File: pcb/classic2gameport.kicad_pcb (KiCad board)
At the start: 2 copper layers, 58 x 45 mm, 39 parts, among them J1 DB15_Male, J2 AVR-ISP-10, J3 Conn_01x04, Q1 Q_PMOS_GSD, Q2 Q_PMOS_GSD, Q3 Q_PMOS_GSD, Q4 Q_PMOS_GSD, Q5 Q_PMOS_GSD, Q6 Q_PMOS_GSD, Q7 Q_PMOS_GSD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

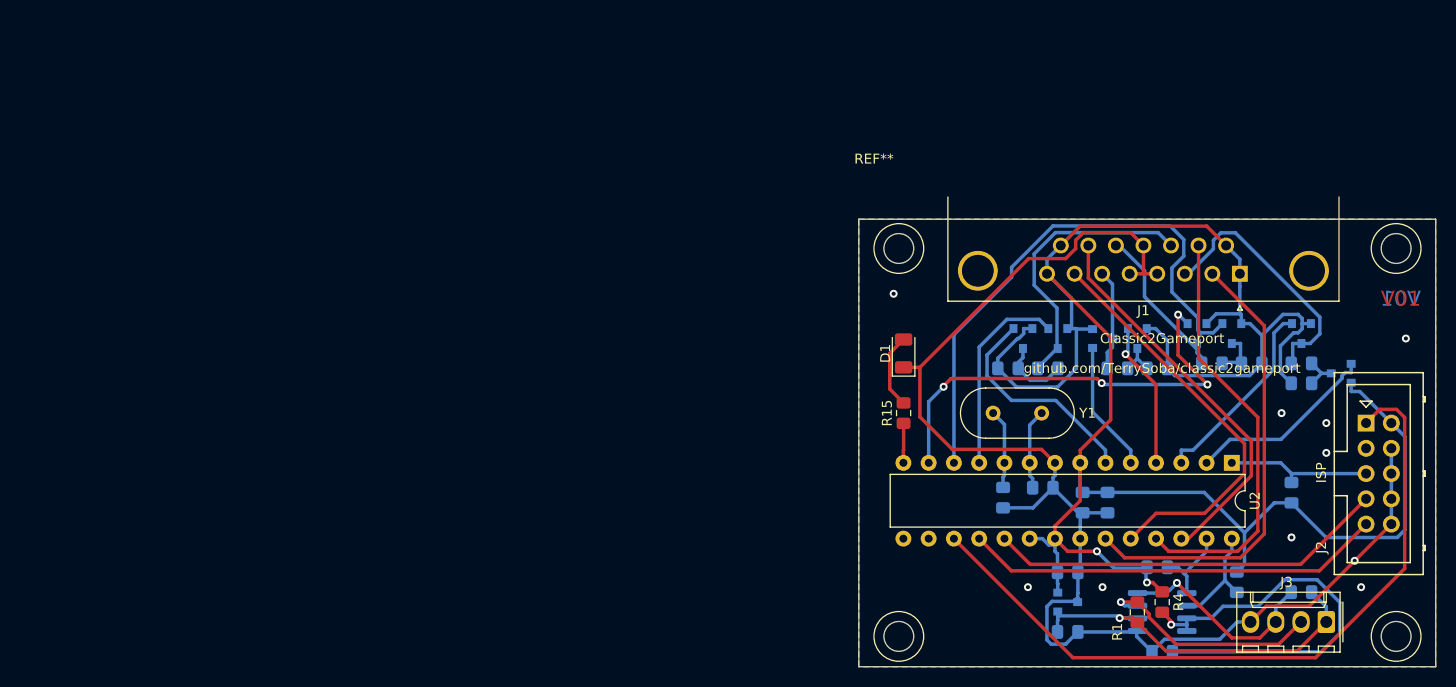
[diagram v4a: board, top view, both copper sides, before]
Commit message: Change to STM32 MCU
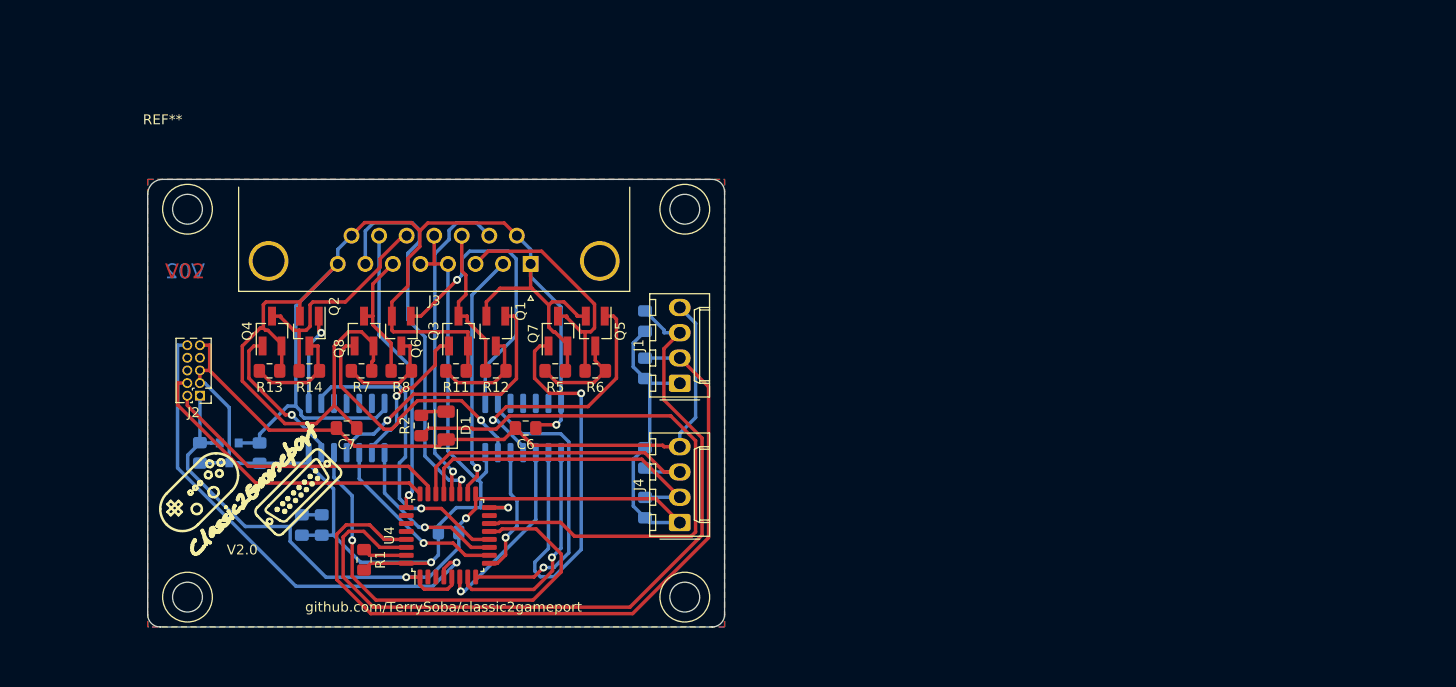
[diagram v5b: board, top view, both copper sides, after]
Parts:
- removed R15: 1.2k, Resistor_SMD:R_0805_2012Metric_Pad1.15x1.40mm_HandSolder
- removed Y1: 16MHz, Crystal:Crystal_HC49-4H_Vertical
- added J4: Conn_01x04, Connector_Molex:Molex_KK-254_AE-6410-04A_1x04_P2.54mm_Vertical, F.Cu at (138.0, 72.0)
- added U4: STM32F030K6Tx, Package_QFP:LQFP-32_7x7mm_P0.8mm, F.Cu at (114.7, 73.3)
- C3: value 22pF -> 1µF
- C4: value 22pF -> 4.7µF
- C6: value 1µF -> 100nF; moved to F.Cu
- C7, R11, R12, R13, R14, R7, R8: moved to F.Cu
- J1: value DB15_Male -> Conn_01x04; footprint Connector_Dsub:DSUB-15_Male_Horizontal_P2.77x2.84mm_EdgePinOffset4.94mm_Housed_MountingHolesOffset7.48mm -> Connector_Molex:Molex_KK-254_AE-6410-04A_1x04_P2.54mm_Vertical
- J2: value AVR-ISP-10 -> Conn_02x05_Odd_Even; footprint Connector_Multicomp:Multicomp_MC9A12-1034_2x05_P2.54mm_Vertical -> Connector_PinHeader_1.27mm:PinHeader_2x05_P1.27mm_Vertical
- J3: value Conn_01x04 -> DB15_Male; footprint Connector_Molex:Molex_KK-254_AE-6410-04A_1x04_P2.54mm_Vertical -> Connector_Dsub:DSUB-15_Male_Horizontal_P2.77x2.84mm_EdgePinOffset4.94mm_Housed_MountingHolesOffset7.48mm
- Q1, Q2, Q3, Q4, Q5, Q6, Q7, Q8: footprint Package_TO_SOT_SMD:SOT-23 -> Package_TO_SOT_SMD:SOT-23_Handsoldering; moved to F.Cu
- R1: value 1kR -> 10k
- R10, R9: value 49k9 -> 1kR
- R2: value 1kR -> 470R; moved to F.Cu
- R3: value 10kR -> 1kR
- R4: value 200kR -> 1kR; moved to B.Cu
- R5, R6: value 1kR -> 49k9; moved to F.Cu
- U1: value LM3480-3.3 -> 74HC14; footprint Package_TO_SOT_SMD:SOT-23 -> Package_SO:SOIC-14_3.9x8.7mm_P1.27mm
- U2: value ATmega8-16PU -> 74HC14; footprint Package_DIP:DIP-28_W7.62mm -> Package_SO:SOIC-14_3.9x8.7mm_P1.27mm; moved to B.Cu
- U3: value PCA9306 -> LM3480-3.3; footprint Package_SO:SOIC-8_3.9x4.9mm_P1.27mm -> Package_TO_SOT_SMD:SOT-23
- moved J2 117.3 mm to (89.8, 59.2), turned to 180 degrees
- moved R13 98.8 mm to (96.8, 56.8)
- moved U3 95.2 mm to (92.7, 65.0), turned to 270 degrees
- moved R7 94.5 mm to (106.0, 56.8), turned to 180 degrees
- moved R14 90.8 mm to (100.8, 56.8)
- moved R8 90.5 mm to (110.0, 56.8)
- moved R2 90.1 mm to (112.0, 62.2), turned to 90 degrees
- moved U2 89.1 mm to (104.5, 62.5), turned to 90 degrees
- moved C2 88.9 mm to (89.8, 65.0)
- moved J3 87.7 mm to (123.0, 46.0)
- moved Q1 85.1 mm to (119.5, 52.8), turned to 270 degrees
- moved C7 85.0 mm to (104.5, 62.5)
- moved Q3 84.8 mm to (115.8, 52.8), turned to 90 degrees
- moved Q8 83.8 mm to (106.2, 52.8), turned to 90 degrees
- moved Q4 83.5 mm to (97.0, 52.8), turned to 90 degrees
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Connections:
- C1 pad 1: 3.3V -> 5V
- C2 pad 1: 5V -> 3.3V
- C3 pad 1: Net-(C3-Pad1) -> 3.3V
- C4 pad 1: GND -> 3.3V
- C4 pad 2: Net-(C4-Pad2) -> GND
- C5 pad 1: 5V -> 3.3V
- C7 pad 1: Net-(C7-Pad1) -> 5V
- J1 pad 1: 5V -> 3.3V
- J1 pad 2: BUTTON1 -> SCL
- J1 pad 3: JS1_X_AXIS -> SDA
- J2 pad 1: MOSI -> 3.3V
- J2 pad 10: GND -> NRST
- J2 pad 2: 5V -> SWDIO
- J2 pad 3: Net-(J2-Pad3) -> GND
- J2 pad 4: GND -> SWCLK
- J2 pad 5: RESET -> GND
- J2 pad 6: GND -> (no net)
- J2 pad 7: SCK -> (no net)
- J2 pad 8: GND -> (no net)
- J2 pad 9: MISO -> GND
- J3 pad 1: 3.3V -> 5V
- J3 pad 2: Net-(J3-Pad2) -> BUTTON1
- J3 pad 3: Net-(J3-Pad3) -> JS1_X_AXIS
- Q1 pad 1: JS1_X1 -> Net-(Q1-Pad1)
- Q2 pad 1: JS1_Y1 -> Net-(Q2-Pad1)
- Q3 pad 1: JS1_X2 -> Net-(Q3-Pad1)
- Q3 pad 3: JS1_X_AXIS -> JS2_X_AXIS
- Q4 pad 1: JS1_Y2 -> Net-(Q4-Pad1)
- Q4 pad 3: JS1_Y_AXIS -> JS2_Y_AXIS
- Q5 pad 1: JS2_X1 -> Net-(Q5-Pad1)
- Q6 pad 1: JS2_Y1 -> Net-(Q6-Pad1)
- Q7 pad 1: JS2_X2 -> Net-(Q7-Pad1)
- Q7 pad 3: JS2_X_AXIS -> JS1_X_AXIS
- Q8 pad 1: JS2_Y2 -> Net-(Q8-Pad1)
- Q8 pad 3: JS2_Y_AXIS -> JS1_Y_AXIS
- R1 pad 1: 3.3V -> Net-(R1-Pad1)
- R1 pad 2: Net-(J3-Pad2) -> GND
- R10 pad 1: Net-(Q2-Pad3) -> 3.3V
- R10 pad 2: JS1_Y_AXIS -> SDA2
- R11 pad 2: Net-(Q5-Pad3) -> Net-(Q1-Pad3)
- R12 pad 1: Net-(Q5-Pad3) -> Net-(Q1-Pad3)
- R13 pad 2: Net-(Q6-Pad3) -> Net-(Q2-Pad3)
- R14 pad 1: Net-(Q6-Pad3) -> Net-(Q2-Pad3)
- R2 pad 1: 3.3V -> Net-(R2-Pad1)
- R2 pad 2: Net-(J3-Pad3) -> Net-(D1-Pad2)
- R3 pad 1: 5V -> 3.3V
- R3 pad 2: RESET -> SCL
- R4 pad 1: 5V -> 3.3V
- R4 pad 2: Net-(C7-Pad1) -> SDA
- R5 pad 2: SCL -> Net-(Q5-Pad3)
- R6 pad 1: 5V -> Net-(Q5-Pad3)
- R6 pad 2: SDA -> JS1_X_AXIS
- R7 pad 2: Net-(Q1-Pad3) -> Net-(Q6-Pad3)
- R8 pad 1: Net-(Q1-Pad3) -> Net-(Q6-Pad3)
- R8 pad 2: JS1_X_AXIS -> JS1_Y_AXIS
- R9 pad 1: 5V -> 3.3V
- R9 pad 2: Net-(Q2-Pad3) -> SCL2
- U1 pad 1: 3.3V -> JS1_X2
- U1 pad 2: 5V -> Net-(Q7-Pad1)
- U1 pad 3: GND -> JS1_X1
- U2 pad 1: RESET -> JS2_X2
- U2 pad 10: Net-(C4-Pad2) -> (no net)
- U2 pad 11: JS2_X2 -> (no net)
- U2 pad 12: JS2_Y1 -> (no net)
- U2 pad 13: JS2_Y2 -> (no net)
- U2 pad 14: Net-(R15-Pad1) -> 5V
- U2 pad 2: JS1_X1 -> Net-(Q3-Pad1)
- U2 pad 3: JS1_X2 -> JS2_X1
- U2 pad 4: JS1_Y1 -> Net-(Q1-Pad1)
- U2 pad 5: JS1_Y2 -> JS2_Y2
- U2 pad 6: JS2_X1 -> Net-(Q4-Pad1)
- U2 pad 7: 5V -> GND
- U2 pad 8: GND -> Net-(Q2-Pad1)
- U2 pad 9: Net-(C3-Pad1) -> JS2_Y1
- U3 pad 1: GND -> 3.3V
- U3 pad 2: 3.3V -> 5V
- U3 pad 3: Net-(J3-Pad2) -> GND
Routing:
- net MOSI: track 74.0 -> 0.00 mm
- net 3.3V: track 37.1 -> 109.4 mm, vias 1 -> 2
- net SDA: track 8.47 -> 78.8 mm
- net SCL: track 11.1 -> 77.3 mm
- net Net-(R2-Pad1): track 0.00 -> 60.2 mm
- net NRST: track 0.00 -> 49.7 mm, vias 0 -> 1
- net Net-(Q7-Pad1): track 0.00 -> 43.9 mm, vias 0 -> 1
- net Net-(C7-Pad1): track 43.1 -> 0.00 mm, vias 1 -> 0
- net MISO: track 42.2 -> 0.00 mm
- net SCK: track 40.2 -> 0.00 mm
- net GND: track 137.1 -> 172.6 mm, vias 10 -> 2
- net 5V: track 213.5 -> 179.3 mm, vias 2 -> 1
- net SDA2: track 0.00 -> 32.3 mm
- net SCL2: track 0.00 -> 31.8 mm
- net SWCLK: track 0.00 -> 31.3 mm
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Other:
- outline, holes or cut-outs redrawn
- board text added: "V02"
- board text added: "V2.0"
- board text removed: "Classic2Gameport"
- board text removed: "ISP"
- board text removed: "V01"

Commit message: Redesign again
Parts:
- removed U3: LM3480-3.3, Package_TO_SOT_SMD:SOT-23
- removed U4: STM32F030K6Tx, Package_QFP:LQFP-32_7x7mm_P0.8mm
- added C8: 100nF, Capacitor_SMD:C_0805_2012Metric_Pad1.15x1.40mm_HandSolder, F.Cu at (107.0, 67.8)
- added Q10: Q_PMOS_GSD, Package_TO_SOT_SMD:SOT-23_Handsoldering, F.Cu at (88.8, 45.5)
- added Q11: Q_PMOS_GSD, Package_TO_SOT_SMD:SOT-23_Handsoldering, F.Cu at (117.2, 50.0)
- added Q12: Q_PMOS_GSD, Package_TO_SOT_SMD:SOT-23_Handsoldering, F.Cu at (87.0, 50.2)
- added Q9: Q_PMOS_GSD, Package_TO_SOT_SMD:SOT-23_Handsoldering, F.Cu at (115.2, 45.3)
- added U5: LM3480-3.3, Package_TO_SOT_SMD:SOT-23, B.Cu at (92.6, 70.9)
- added U8: STM32F030K6Tx, Package_QFP:LQFP-32_7x7mm_P0.8mm, F.Cu at (101.5, 63.0)
- C3: value 1µF -> 100nF; moved to F.Cu
- C4: value 4.7µF -> 1µF; moved to F.Cu
- C5: value 100nF -> 4.7µF; moved to F.Cu
- J2: value Conn_02x05_Odd_Even -> Conn_01x04; footprint Connector_PinHeader_1.27mm:PinHeader_2x05_P1.27mm_Vertical -> Connector_Molex:Molex_KK-254_AE-6410-04A_1x04_P2.54mm_Vertical
- J3: value DB15_Male -> Conn_02x05_Odd_Even; footprint Connector_Dsub:DSUB-15_Male_Horizontal_P2.77x2.84mm_EdgePinOffset4.94mm_Housed_MountingHolesOffset7.48mm -> Connector_PinHeader_1.27mm:PinHeader_2x05_P1.27mm_Vertical
- J4: value Conn_01x04 -> DB15_Male; footprint Connector_Molex:Molex_KK-254_AE-6410-04A_1x04_P2.54mm_Vertical -> Connector_Dsub:DSUB-15_Male_Horizontal_P2.77x2.84mm_EdgePinOffset4.94mm_Housed_MountingHolesOffset7.48mm
- R1: value 10k -> 1kR; moved to B.Cu
- R10: value 1kR -> 470R
- R11, R12, R13, R14, R7, R8: value 49k9 -> 100kR
- R2: value 470R -> 1kR; moved to B.Cu
- R3, R4: value 1kR -> 100kR; moved to F.Cu
- R5, R6: value 49k9 -> 1kR; moved to B.Cu
- R9: value 1kR -> 10k; moved to F.Cu
- U1, U2: moved to F.Cu
- moved R10 62.6 mm to (75.8, 43.8), turned to 90 degrees
- moved J3 46.6 mm to (77.8, 57.2)
- moved J4 45.9 mm to (111.5, 34.5), turned to 180 degrees
- moved D1 45.5 mm to (75.8, 38.4), turned to 270 degrees
- moved R4 40.0 mm to (96.1, 40.5)
- moved J2 37.3 mm to (127.0, 61.0), turned to 90 degrees
- moved R12 37.2 mm to (85.9, 40.8), turned to 90 degrees
- moved U1 37.0 mm to (85.2, 62.0), turned to 180 degrees
- moved R1 34.6 mm to (123.5, 45.8), turned to 0 degrees
- moved R3 33.8 mm to (104.7, 40.5)
- moved R9 33.5 mm to (101.0, 71.0), turned to 0 degrees
- moved C5 26.0 mm to (96.0, 55.0), turned to 0 degrees
- moved R13 25.2 mm to (116.0, 40.5), turned to 90 degrees
- moved Q5 23.7 mm to (106.0, 50.0), turned to 180 degrees
- moved Q8 22.4 mm to (85.1, 45.5)
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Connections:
- C1 pad 1: 5V -> 3.3V
- C2 pad 1: 3.3V -> 5V
- J1 pad 2: SCL -> SCL2
- J1 pad 3: SDA -> SDA2
- J2 pad 2: SWDIO -> SCL
- J2 pad 3: GND -> SDA
- J2 pad 4: SWCLK -> GND
- J3 pad 1: 5V -> 3.3V
- J3 pad 10: BUTTON3 -> NRST
- J3 pad 2: BUTTON1 -> SWDIO
- J3 pad 3: JS1_X_AXIS -> GND
- J3 pad 4: GND -> SWCLK
- J3 pad 6: JS1_Y_AXIS -> (no net)
- J3 pad 7: BUTTON2 -> (no net)
- J3 pad 8: 5V -> (no net)
- J3 pad 9: 5V -> GND
- J4 pad 1: 3.3V -> 5V
- J4 pad 2: SCL2 -> BUTTON1
- J4 pad 3: SDA2 -> JS1_X_AXIS
- Q3 pad 3: JS2_X_AXIS -> Net-(Q3-Pad3)
- Q4 pad 3: JS2_Y_AXIS -> Net-(Q4-Pad3)
- Q5 pad 3: Net-(Q5-Pad3) -> JS1_X_AXIS
- Q6 pad 3: Net-(Q6-Pad3) -> JS1_Y_AXIS
- Q7 pad 3: JS1_X_AXIS -> Net-(Q7-Pad3)
- Q8 pad 3: JS1_Y_AXIS -> Net-(Q8-Pad3)
- R1 pad 1: Net-(R1-Pad1) -> 3.3V
- R1 pad 2: GND -> SCL2
- R10 pad 1: 3.3V -> Net-(R10-Pad1)
- R10 pad 2: SDA2 -> Net-(D1-Pad2)
- R11 pad 1: 5V -> Net-(Q7-Pad3)
- R11 pad 2: Net-(Q1-Pad3) -> JS2_X_AXIS
- R12 pad 1: Net-(Q1-Pad3) -> Net-(Q8-Pad3)
- R12 pad 2: JS2_X_AXIS -> JS2_Y_AXIS
- R13 pad 1: 5V -> Net-(Q9-Pad3)
- R13 pad 2: Net-(Q2-Pad3) -> JS2_X_AXIS
- R14 pad 1: Net-(Q2-Pad3) -> Net-(Q10-Pad3)
- R2 pad 1: Net-(R2-Pad1) -> 3.3V
- R2 pad 2: Net-(D1-Pad2) -> SCL
- R3 pad 1: 3.3V -> Net-(Q1-Pad3)
- R3 pad 2: SCL -> JS1_X_AXIS
- R4 pad 1: 3.3V -> Net-(Q2-Pad3)
- R4 pad 2: SDA -> JS1_Y_AXIS
- R5 pad 1: 5V -> 3.3V
- R5 pad 2: Net-(Q5-Pad3) -> SDA2
- R6 pad 1: Net-(Q5-Pad3) -> 3.3V
- R6 pad 2: JS1_X_AXIS -> SDA
- R7 pad 1: 5V -> Net-(Q3-Pad3)
- R7 pad 2: Net-(Q6-Pad3) -> JS1_X_AXIS
- R8 pad 1: Net-(Q6-Pad3) -> Net-(Q4-Pad3)
- R9 pad 1: 3.3V -> Net-(R9-Pad1)
- R9 pad 2: SCL2 -> GND
- U1 pad 1: JS1_X2 -> JS1_X1
- U1 pad 10: (no net) -> Net-(Q4-Pad1)
- U1 pad 11: (no net) -> JS1_Y2
- U1 pad 12: (no net) -> Net-(Q6-Pad1)
- U1 pad 13: (no net) -> JS1_Y3
- U1 pad 2: Net-(Q7-Pad1) -> Net-(Q1-Pad1)
- U1 pad 3: JS1_X1 -> JS1_X2
- U1 pad 4: Net-(Q5-Pad1) -> Net-(Q3-Pad1)
- U1 pad 5: JS1_Y2 -> JS1_X3
- U1 pad 6: Net-(Q8-Pad1) -> Net-(Q5-Pad1)
- U1 pad 8: Net-(Q6-Pad1) -> Net-(Q2-Pad1)
- U2 pad 1: JS2_X2 -> JS2_X1
- U2 pad 10: (no net) -> Net-(Q10-Pad1)
- U2 pad 11: (no net) -> JS2_Y2
- U2 pad 12: (no net) -> Net-(Q12-Pad1)
- U2 pad 13: (no net) -> JS2_Y3
- U2 pad 2: Net-(Q3-Pad1) -> Net-(Q7-Pad1)
- U2 pad 3: JS2_X1 -> JS2_X2
- U2 pad 4: Net-(Q1-Pad1) -> Net-(Q9-Pad1)
- U2 pad 5: JS2_Y2 -> JS2_X3
- U2 pad 6: Net-(Q4-Pad1) -> Net-(Q11-Pad1)
- U2 pad 8: Net-(Q2-Pad1) -> Net-(Q8-Pad1)
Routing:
- net Net-(Q12-Pad1): track 0.00 -> 77.8 mm, vias 0 -> 2
- net Net-(Q10-Pad1): track 0.00 -> 72.6 mm, vias 0 -> 2
- net Net-(R2-Pad1): track 60.2 -> 0.00 mm
- net GND: track 172.6 -> 230.5 mm
- net JS1_Y3: track 0.00 -> 47.2 mm, vias 0 -> 2
- net Net-(R10-Pad1): track 0.00 -> 45.9 mm, vias 0 -> 3
- net Net-(Q8-Pad1): track 27.1 -> 70.9 mm, vias 1 -> 2
- net SDA: track 78.8 -> 35.7 mm, vias 0 -> 1
- net JS1_Y2: track 13.0 -> 55.3 mm, vias 1 -> 2
- net SCL: track 77.3 -> 44.1 mm, vias 0 -> 2
- net SDA2: track 32.3 -> 62.2 mm, vias 0 -> 2
- net JS2_Y2: track 46.6 -> 17.9 mm, vias 1 -> 2
- net JS1_X2: track 22.6 -> 46.7 mm, vias 1 -> 2
- net JS2_X3: track 0.00 -> 24.0 mm
- net BUTTON4: track 29.0 -> 51.4 mm
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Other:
- outline, holes or cut-outs redrawn
- board text added: "V03"
- board text added: "V3.0"
- board text removed: "V02"
- board text removed: "V2.0"

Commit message: Version 4.0 of PCB
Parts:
- removed C8: 100nF, Capacitor_SMD:C_0805_2012Metric_Pad1.15x1.40mm_HandSolder
- removed R10: 470R, Resistor_SMD:R_0805_2012Metric_Pad1.15x1.40mm_HandSolder
- removed U8: STM32F030K6Tx, Package_QFP:LQFP-32_7x7mm_P0.8mm
- added C10: 100nF, Capacitor_SMD:C_0805_2012Metric_Pad1.15x1.40mm_HandSolder, F.Cu at (94.0, 65.5)
- added C9: 4.7µF, Capacitor_SMD:C_0805_2012Metric_Pad1.15x1.40mm_HandSolder, B.Cu at (88.5, 70.0)
- added U3: STM32G071KxT, Package_QFP:LQFP-32_7x7mm_P0.8mm, F.Cu at (101.5, 63.0)
- C5: moved to B.Cu
- R9: value 10k -> 470R
- moved R9 37.9 mm to (75.8, 42.8), turned to 90 degrees
- moved C4 18.0 mm to (93.0, 62.5), turned to 270 degrees
- moved C5 15.2 mm to (98.2, 70.0), turned to 90 degrees
- moved C3 4.34 mm to (95.0, 62.5), turned to 270 degrees
- moved C1 1.06 mm to (96.2, 70.0)
- moved C2 1.06 mm to (90.5, 70.0)
- moved U5 1.06 mm to (93.3, 70.2)
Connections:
- J3 pad 6: (no net) -> Net-(J3-Pad6)
- J3 pad 7: (no net) -> Net-(J3-Pad7)
- J3 pad 8: (no net) -> Net-(J3-Pad8)
- R9 pad 2: GND -> Net-(D1-Pad2)
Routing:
- net Net-(R10-Pad1): track 45.9 -> 0.00 mm, vias 3 -> 0
- net Net-(Q12-Pad1): track 77.8 -> 34.2 mm
- net Net-(R9-Pad1): track 6.19 -> 44.4 mm
- net Net-(Q10-Pad1): track 72.6 -> 35.9 mm, vias 2 -> 0
- net GND: track 230.5 -> 195.2 mm, vias 2 -> 15
- net JS1_X2: track 46.7 -> 12.0 mm
- net Net-(Q8-Pad1): track 70.9 -> 37.0 mm
- net SDA2: track 62.2 -> 32.3 mm, vias 2 -> 1
- net JS1_Y2: track 55.3 -> 28.9 mm
- net BUTTON4: track 51.4 -> 30.4 mm
- net Net-(Q6-Pad1): track 43.0 -> 23.3 mm, vias 0 -> 2
- net 5V: track 193.6 -> 174.3 mm, vias 2 -> 5
- net JS1_Y3: track 47.2 -> 28.4 mm, vias 2 -> 0
- net SCL2: track 43.5 -> 30.5 mm
- net JS1_X_AXIS: track 18.7 -> 30.3 mm
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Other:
- board text added: "V04"
- board text added: "V4.0"
- board text removed: "V03"
- board text removed: "V3.0"
